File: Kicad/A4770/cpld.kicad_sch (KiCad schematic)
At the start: 31 parts, among them J8 Conn_01x06_Pin, U13 W25X40CLSN, U7 AMS1117-3.3, U8 XC95144XL-TQ144, Y1 Abracon ACO-50MHz, Y2 Abracon ACO-40MHz

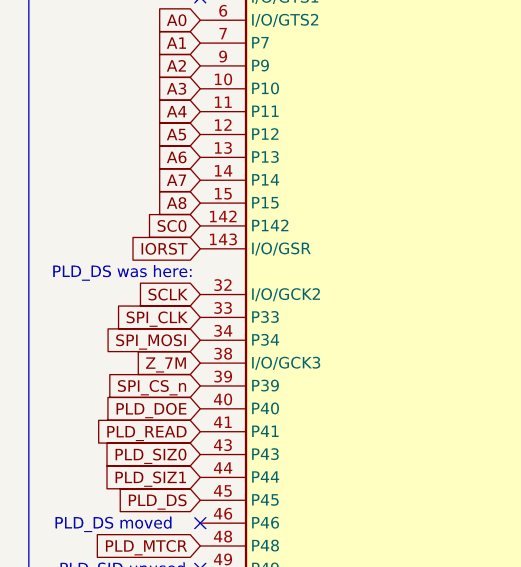
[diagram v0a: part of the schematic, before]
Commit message: Remove SCLK from CPLD
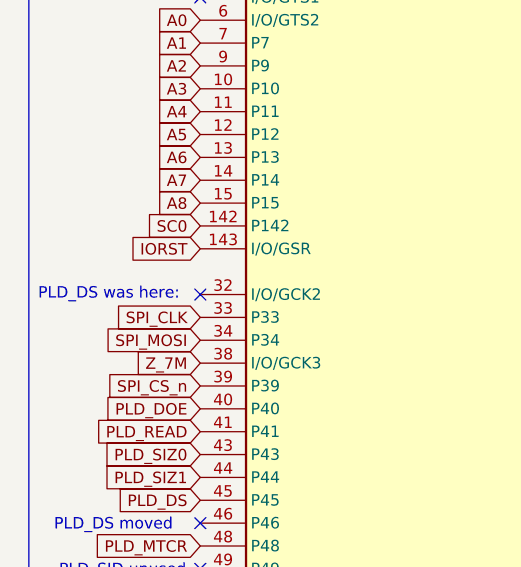
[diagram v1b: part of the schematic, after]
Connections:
- net SCLK: no longer U8.32 (I/O/GCK2)
- no-connect marks 11 -> 12
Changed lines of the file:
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@@
 	(text "PLD_DS was here:"
 		(exclude_from_sim no)
-		(at 25.654 101.854 0)
+		(at 24.13 104.14 0)
 		(effects
 			(font
@@
 	)
 	(no_connect
+		(at 34.29 104.14)
+	)
+	(no_connect
 		(at 34.29 66.04)
 	)
@@
 				(hide yes)
 			)
-		)
-	)
-	(global_label "SCLK"
-		(shape input)
-		(at 34.29 104.14 180)
-		(fields_autoplaced yes)
-		(effects
-			(font
-				(size 1.27 1.27)
-			)
-			(justify right)
-		)
-		(property "Intersheetrefs" "${INTERSHEET_REFS}"
-			(at 26.5272 104.14 0)
-			(effects
-				(font
-					(size 1.27 1.27)
-				)
-				(justify right)
-				(hide yes)
-			)

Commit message: Fix issues detected by JLCPCB's uploader
- Use alternating decoupling caps of 0.01uF and 0.1uF on the
  NCR53c770 as was done on the A4091 design.
- Remove DNP parts from BOM
- Remove fiducials from position files.
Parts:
- J8, R81, R82, R84: now left out of the parts list
- R83: footprint R131 -> Resistor_SMD:R_0603_1608Metric_Pad0.98x0.95mm_HandSolder; now left out of the parts list
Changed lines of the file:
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@@
 		(unit 1)
 		(exclude_from_sim no)
-		(in_bom yes)
+		(in_bom no)
 		(on_board yes)
 		(dnp yes)
@@
 		(unit 1)
 		(exclude_from_sim no)
-		(in_bom yes)
+		(in_bom no)
 		(on_board yes)
 		(dnp yes)
@@
 		(unit 1)
 		(exclude_from_sim no)
-		(in_bom yes)
+		(in_bom no)
 		(on_board yes)
 		(dnp yes)
@@
 		(unit 1)
 		(exclude_from_sim no)
-		(in_bom yes)
+		(in_bom no)
 		(on_board yes)
 		(dnp yes)
@@
 			)
 		)
-		(property "Footprint" "R131"
+		(property "Footprint" "Resistor_SMD:R_0603_1608Metric_Pad0.98x0.95mm_HandSolder"
 			(at 163.83 33.02 0)
 			(effects
@@
 		(unit 1)
 		(exclude_from_sim no)
-		(in_bom yes)
+		(in_bom no)
 		(on_board yes)
 		(dnp yes)

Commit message: Fix footprints
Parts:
- U8: footprint 144-TQFP_XIL -> Package_QFP:TQFP-144_20x20mm_P0.5mm
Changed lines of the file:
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@@
 			)
 		)
-		(property "Footprint" "144-TQFP_XIL"
+		(property "Footprint" "Package_QFP:TQFP-144_20x20mm_P0.5mm"
 			(at 67.31 104.14 0)
 			(effects
